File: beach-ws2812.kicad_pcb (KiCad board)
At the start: 4 copper layers, 260 x 120 mm, 183 parts, among them CON101 BARREL_JACK, P101 CONN_01X03, SW101 Pushbutton, SW102 Pushbutton, U101 STM32F103C(8-B)Tx, U102 LM1117-3.3, U103 MAX811, X101 8MHz

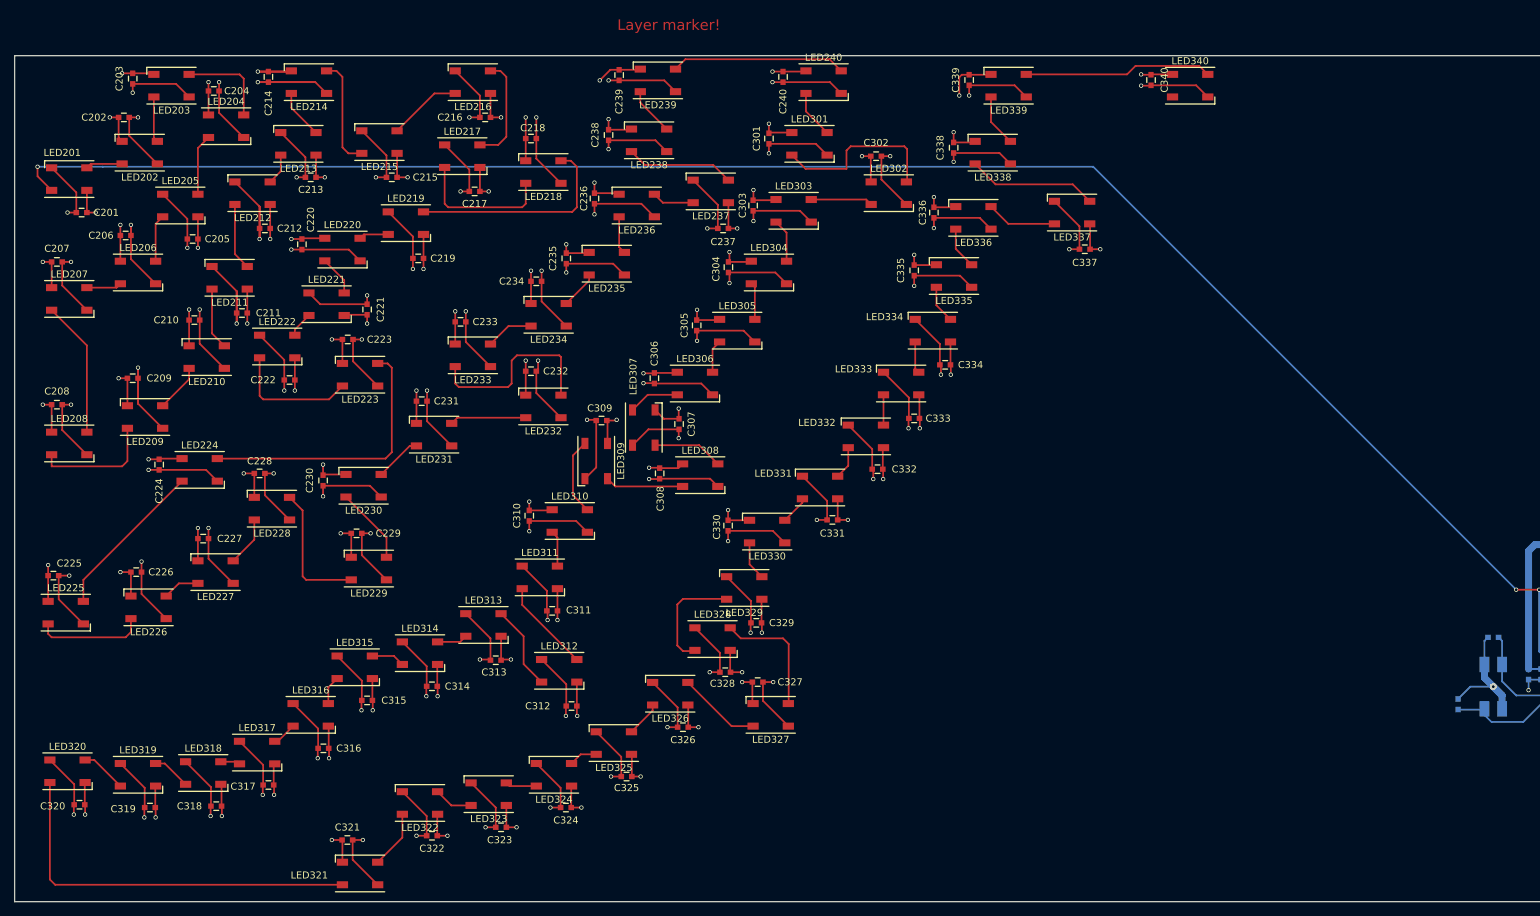
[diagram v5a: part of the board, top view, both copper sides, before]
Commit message: Now with 120 LEDs routed.
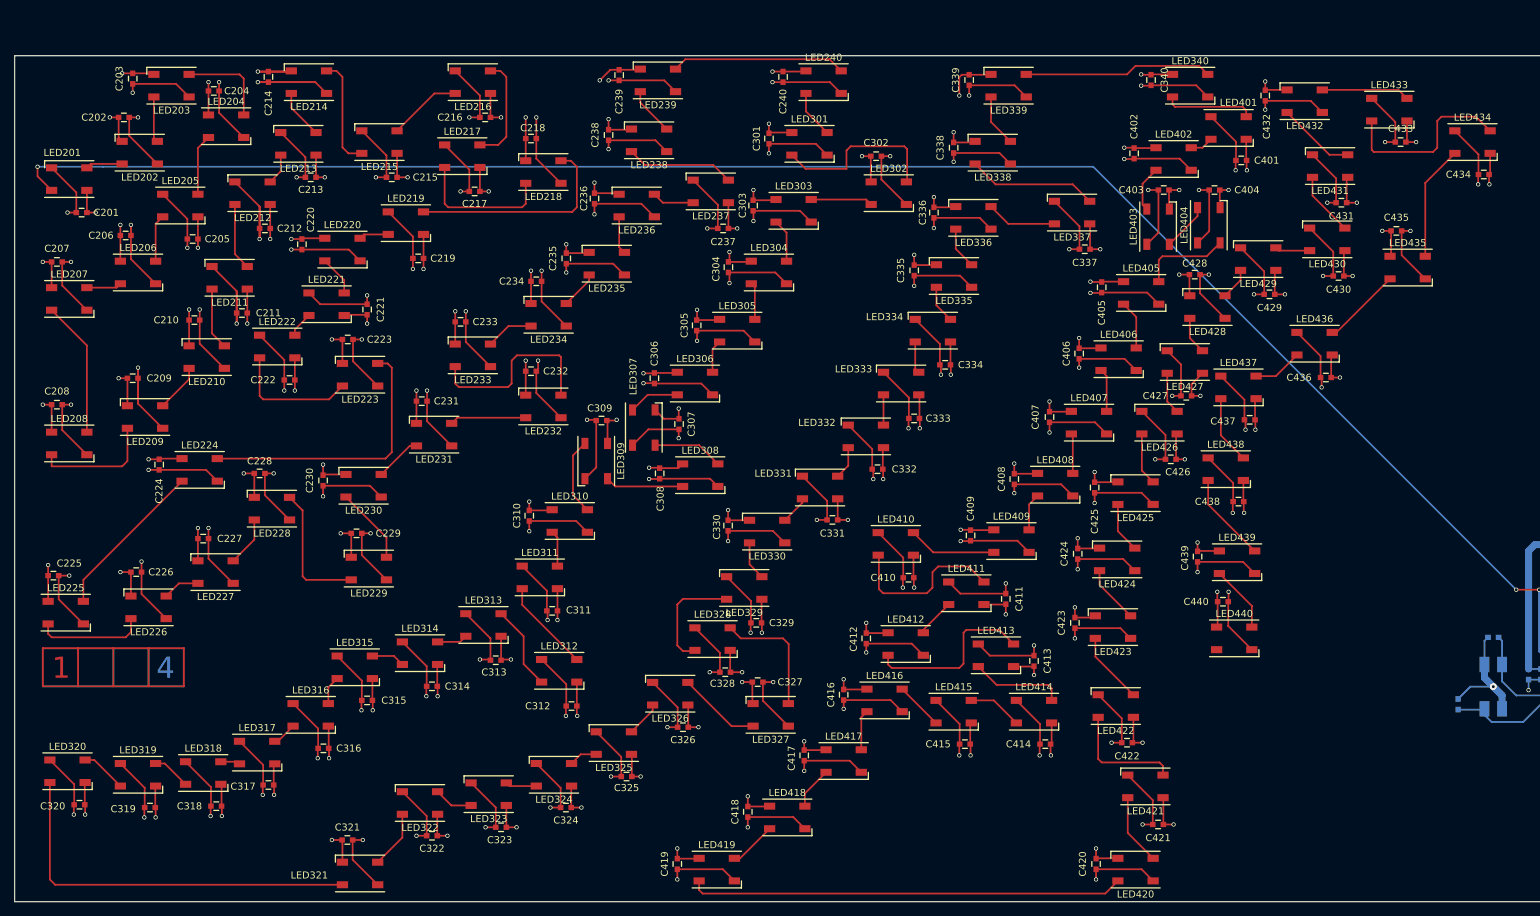
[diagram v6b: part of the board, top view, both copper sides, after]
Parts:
- added C401: 100nF, Capacitors_SMD:C_0603, F.Cu at (194.0, 33.6)
- added C402: 100nF, Capacitors_SMD:C_0603, F.Cu at (178.8, 32.6)
- added C403: 100nF, Capacitors_SMD:C_0603, F.Cu at (183.0, 37.8)
- added C404: 100nF, Capacitors_SMD:C_0603, F.Cu at (190.2, 37.8)
- added C405: 100nF, Capacitors_SMD:C_0603, F.Cu at (174.2, 51.6)
- added C406: 100nF, Capacitors_SMD:C_0603, F.Cu at (171.0, 61.0)
- added C407: 100nF, Capacitors_SMD:C_0603, F.Cu at (166.8, 70.0)
- added C408: 100nF, Capacitors_SMD:C_0603, F.Cu at (161.8, 78.8)
- added C409: 100nF, Capacitors_SMD:C_0603, F.Cu at (155.6, 86.8)
- added C410: 100nF, Capacitors_SMD:C_0603, F.Cu at (146.8, 92.8)
- added C411: 100nF, Capacitors_SMD:C_0603, F.Cu at (160.6, 95.8)
- added C412: 100nF, Capacitors_SMD:C_0603, F.Cu at (140.8, 101.4)
- added C413: 100nF, Capacitors_SMD:C_0603, F.Cu at (164.6, 104.6)
- added C414: 100nF, Capacitors_SMD:C_0603, F.Cu at (166.2, 116.4)
- added C415: 100nF, Capacitors_SMD:C_0603, F.Cu at (154.8, 116.4)
- added C416: 100nF, Capacitors_SMD:C_0603, F.Cu at (137.6, 109.4)
- added C417: 100nF, Capacitors_SMD:C_0603, F.Cu at (132.0, 118.0)
- added C418: 100nF, Capacitors_SMD:C_0603, F.Cu at (124.0, 126.0)
- added C419: 100nF, Capacitors_SMD:C_0603, F.Cu at (114.0, 133.4)
- added C420: 100nF, Capacitors_SMD:C_0603, F.Cu at (173.4, 133.4)
- added C421: 100nF, Capacitors_SMD:C_0603, F.Cu at (182.2, 127.8)
- added C422: 100nF, Capacitors_SMD:C_0603, F.Cu at (177.8, 116.2)
- added C423: 100nF, Capacitors_SMD:C_0603, F.Cu at (170.4, 99.2)
- added C424: 100nF, Capacitors_SMD:C_0603, F.Cu at (170.8, 89.4)
- added C425: 100nF, Capacitors_SMD:C_0603, F.Cu at (173.2, 80.0)
- added C426: 100nF, Capacitors_SMD:C_0603, F.Cu at (184.0, 76.0)
- added C427: 100nF, Capacitors_SMD:C_0603, F.Cu at (186.2, 67.0)
- added C428: 100nF, Capacitors_SMD:C_0603, F.Cu at (187.4, 49.8)
- added C429: 100nF, Capacitors_SMD:C_0603, F.Cu at (198.0, 52.6)
- added C430: 100nF, Capacitors_SMD:C_0603, F.Cu at (207.8, 50.0)
- added C431: 100nF, Capacitors_SMD:C_0603, F.Cu at (208.2, 39.6)
- added C432: 100nF, Capacitors_SMD:C_0603, F.Cu at (197.4, 24.4)
- added C433: 100nF, Capacitors_SMD:C_0603, F.Cu at (216.6, 31.0)
- added C434: 100nF, Capacitors_SMD:C_0603, F.Cu at (228.4, 35.6)
- added C435: 100nF, Capacitors_SMD:C_0603, F.Cu at (216.0, 43.6)
- added C436: 100nF, Capacitors_SMD:C_0603, F.Cu at (206.0, 64.4)
- added C437: 100nF, Capacitors_SMD:C_0603, F.Cu at (195.2, 70.4)
- added C438: 100nF, Capacitors_SMD:C_0603, F.Cu at (193.6, 82.0)
- added C439: 100nF, Capacitors_SMD:C_0603, F.Cu at (187.8, 89.8)
- added C440: 100nF, Capacitors_SMD:C_0603, F.Cu at (191.4, 96.2)
- added LED401: WS2812B, LEDs:LED_WS2812B-PLCC4, F.Cu at (192.2, 29.0)
- added LED402: WS2812B, LEDs:LED_WS2812B-PLCC4, F.Cu at (184.4, 33.4)
- added LED403: WS2812B, LEDs:LED_WS2812B-PLCC4, F.Cu at (182.2, 43.0)
- added LED404: WS2812B, LEDs:LED_WS2812B-PLCC4, F.Cu at (189.4, 42.8)
- added LED405: WS2812B, LEDs:LED_WS2812B-PLCC4, F.Cu at (179.8, 52.4)
- added LED406: WS2812B, LEDs:LED_WS2812B-PLCC4, F.Cu at (176.6, 61.8)
- added LED407: WS2812B, LEDs:LED_WS2812B-PLCC4, F.Cu at (172.4, 70.8)
- added LED408: WS2812B, LEDs:LED_WS2812B-PLCC4, F.Cu at (167.6, 79.6)
- added LED409: WS2812B, LEDs:LED_WS2812B-PLCC4, F.Cu at (161.4, 87.6)
- added LED410: WS2812B, LEDs:LED_WS2812B-PLCC4, F.Cu at (145.0, 88.0)
- added LED411: WS2812B, LEDs:LED_WS2812B-PLCC4, F.Cu at (155.0, 95.0)
- added LED412: WS2812B, LEDs:LED_WS2812B-PLCC4, F.Cu at (146.4, 102.2)
- added LED413: WS2812B, LEDs:LED_WS2812B-PLCC4, F.Cu at (159.2, 103.8)
- added LED414: WS2812B, LEDs:LED_WS2812B-PLCC4, F.Cu at (164.6, 111.8)
- added LED415: WS2812B, LEDs:LED_WS2812B-PLCC4, F.Cu at (153.2, 111.8)
- added LED416: WS2812B, LEDs:LED_WS2812B-PLCC4, F.Cu at (143.4, 110.2)
- added LED417: WS2812B, LEDs:LED_WS2812B-PLCC4, F.Cu at (137.6, 118.8)
- added LED418: WS2812B, LEDs:LED_WS2812B-PLCC4, F.Cu at (129.6, 126.8)
- added LED419: WS2812B, LEDs:LED_WS2812B-PLCC4, F.Cu at (119.6, 134.2)
- added LED420: WS2812B, LEDs:LED_WS2812B-PLCC4, F.Cu at (179.0, 134.2)
- added LED421: WS2812B, LEDs:LED_WS2812B-PLCC4, F.Cu at (180.4, 122.4)
- added LED422: WS2812B, LEDs:LED_WS2812B-PLCC4, F.Cu at (176.2, 111.0)
- added LED423: WS2812B, LEDs:LED_WS2812B-PLCC4, F.Cu at (175.8, 99.8)
- added LED424: WS2812B, LEDs:LED_WS2812B-PLCC4, F.Cu at (176.4, 90.2)
- added LED425: WS2812B, LEDs:LED_WS2812B-PLCC4, F.Cu at (179.0, 80.8)
- added LED426: WS2812B, LEDs:LED_WS2812B-PLCC4, F.Cu at (182.4, 70.8)
- added LED427: WS2812B, LEDs:LED_WS2812B-PLCC4, F.Cu at (186.0, 62.2)
- added LED428: WS2812B, LEDs:LED_WS2812B-PLCC4, F.Cu at (189.2, 54.4)
- added LED429: WS2812B, LEDs:LED_WS2812B-PLCC4, F.Cu at (196.4, 47.6)
- added LED430: WS2812B, LEDs:LED_WS2812B-PLCC4, F.Cu at (206.2, 44.8)
- added LED431: WS2812B, LEDs:LED_WS2812B-PLCC4, F.Cu at (206.6, 34.4)
- added LED432: WS2812B, LEDs:LED_WS2812B-PLCC4, F.Cu at (203.0, 25.2)
- added LED433: WS2812B, LEDs:LED_WS2812B-PLCC4, F.Cu at (215.0, 26.4)
- added LED434: WS2812B, LEDs:LED_WS2812B-PLCC4, F.Cu at (226.8, 31.0)
- added LED435: WS2812B, LEDs:LED_WS2812B-PLCC4, F.Cu at (217.6, 48.8)
- added LED436: WS2812B, LEDs:LED_WS2812B-PLCC4, F.Cu at (204.4, 59.6)
- added LED437: WS2812B, LEDs:LED_WS2812B-PLCC4, F.Cu at (193.6, 65.8)
- added LED438: WS2812B, LEDs:LED_WS2812B-PLCC4, F.Cu at (191.8, 77.4)
- added LED439: WS2812B, LEDs:LED_WS2812B-PLCC4, F.Cu at (193.4, 90.6)
- added LED440: WS2812B, LEDs:LED_WS2812B-PLCC4, F.Cu at (193.0, 101.4)
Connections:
- LED340 pad 2: Net-(LED340-Pad2) -> LEDDATA3
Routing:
- net GND: track 731.1 -> 1032.6 mm, vias 91 -> 131
- net +5V: track 671.5 -> 962.5 mm, vias 81 -> 121
- net (no net): track 0.50 -> 268.0 mm
- net Net-(LED419-Pad2): track 0.00 -> 61.7 mm
- net Net-(LED433-Pad2): track 0.00 -> 26.1 mm
- net Net-(LED412-Pad2): track 0.00 -> 24.9 mm
- net Net-(LED410-Pad2): track 0.00 -> 23.8 mm
- net Net-(LED421-Pad2): track 0.00 -> 16.8 mm
- net Net-(LED434-Pad2): track 0.00 -> 16.3 mm
- net Net-(LED413-Pad2): track 0.00 -> 13.4 mm
- net Net-(LED404-Pad2): track 0.00 -> 12.8 mm
- net LEDDATA3: track 0.00 -> 12.8 mm
- net Net-(LED438-Pad2): track 0.00 -> 12.7 mm
- net Net-(LED409-Pad2): track 0.00 -> 12.6 mm
- net Net-(LED432-Pad2): track 0.00 -> 12.5 mm
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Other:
- board text added: "1"
- board text added: "2"
- board text added: "3"
- board text added: "4"
- board text removed: "Layer marker!"

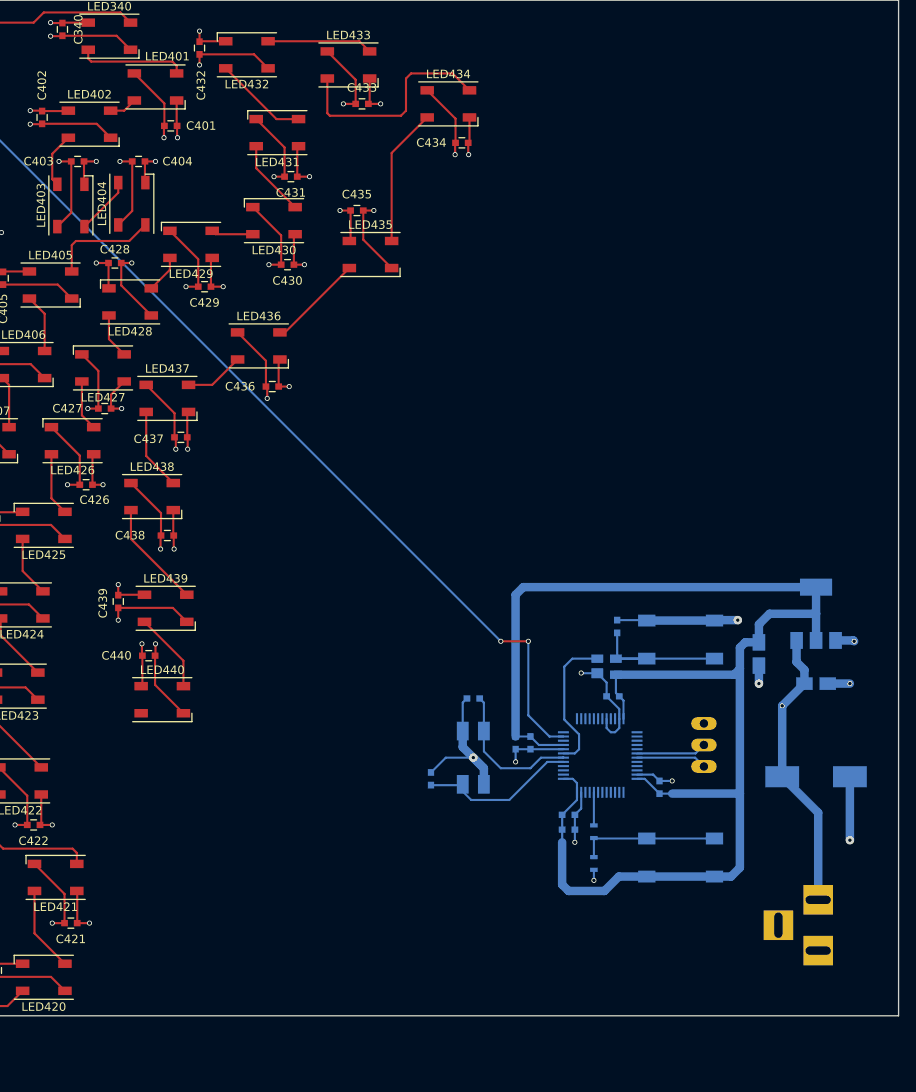
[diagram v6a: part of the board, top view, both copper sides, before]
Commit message: Placed 160 LEDs (caps missing for the last 40).
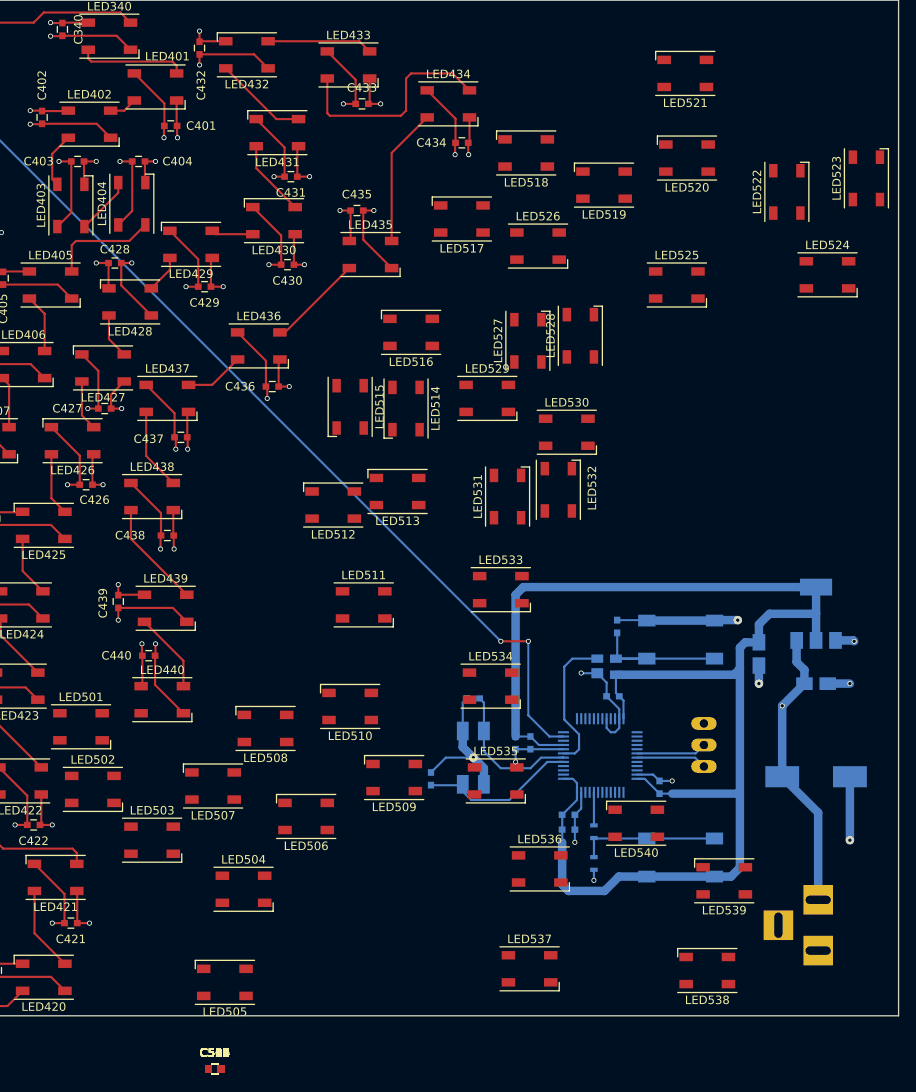
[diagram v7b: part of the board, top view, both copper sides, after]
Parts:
- added C501, C502, C503, C504, C505, C506, C507, C508, C509, C510, C511, C512, C513, C514, C515, C516, C517, C518, C519, C520, C521, C522, C523, C524, C525, C526, C527, C528, C529, C530, C531, C532, C533, C534, C535, C536, C537, C538, C539, C540: 100nF, Capacitors_SMD:C_0603, F.Cu at (199.2, 145.0)
- added LED501: WS2812B, LEDs:LED_WS2812B-PLCC4, F.Cu at (183.4, 104.6)
- added LED502: WS2812B, LEDs:LED_WS2812B-PLCC4, F.Cu at (184.8, 112.0)
- added LED503: WS2812B, LEDs:LED_WS2812B-PLCC4, F.Cu at (191.8, 118.0)
- added LED504: WS2812B, LEDs:LED_WS2812B-PLCC4, F.Cu at (202.6, 123.8)
- added LED505: WS2812B, LEDs:LED_WS2812B-PLCC4, F.Cu at (200.4, 134.8)
- added LED506: WS2812B, LEDs:LED_WS2812B-PLCC4, F.Cu at (210.0, 115.2)
- added LED507: WS2812B, LEDs:LED_WS2812B-PLCC4, F.Cu at (199.0, 111.6)
- added LED508: WS2812B, LEDs:LED_WS2812B-PLCC4, F.Cu at (205.2, 104.8)
- added LED509: WS2812B, LEDs:LED_WS2812B-PLCC4, F.Cu at (220.4, 110.6)
- added LED510: WS2812B, LEDs:LED_WS2812B-PLCC4, F.Cu at (215.2, 102.2)
- added LED511: WS2812B, LEDs:LED_WS2812B-PLCC4, F.Cu at (216.8, 90.2)
- added LED512: WS2812B, LEDs:LED_WS2812B-PLCC4, F.Cu at (213.2, 78.4)
- added LED513: WS2812B, LEDs:LED_WS2812B-PLCC4, F.Cu at (220.8, 76.8)
- added LED514: WS2812B, LEDs:LED_WS2812B-PLCC4, F.Cu at (221.8, 67.0)
- added LED515: WS2812B, LEDs:LED_WS2812B-PLCC4, F.Cu at (215.2, 66.8)
- added LED516: WS2812B, LEDs:LED_WS2812B-PLCC4, F.Cu at (222.4, 58.0)
- added LED517: WS2812B, LEDs:LED_WS2812B-PLCC4, F.Cu at (228.4, 44.6)
- added LED518: WS2812B, LEDs:LED_WS2812B-PLCC4, F.Cu at (236.0, 36.8)
- added LED519: WS2812B, LEDs:LED_WS2812B-PLCC4, F.Cu at (245.2, 40.6)
- added LED520: WS2812B, LEDs:LED_WS2812B-PLCC4, F.Cu at (255.0, 37.4)
- added LED521: WS2812B, LEDs:LED_WS2812B-PLCC4, F.Cu at (254.8, 27.4)
- added LED522: WS2812B, LEDs:LED_WS2812B-PLCC4, F.Cu at (266.8, 41.4)
- added LED523: WS2812B, LEDs:LED_WS2812B-PLCC4, F.Cu at (276.2, 39.8)
- added LED524: WS2812B, LEDs:LED_WS2812B-PLCC4, F.Cu at (271.6, 51.2)
- added LED525: WS2812B, LEDs:LED_WS2812B-PLCC4, F.Cu at (253.8, 52.4)
- added LED526: WS2812B, LEDs:LED_WS2812B-PLCC4, F.Cu at (237.4, 47.8)
- added LED527: WS2812B, LEDs:LED_WS2812B-PLCC4, F.Cu at (236.2, 59.0)
- added LED528: WS2812B, LEDs:LED_WS2812B-PLCC4, F.Cu at (242.4, 58.4)
- added LED529: WS2812B, LEDs:LED_WS2812B-PLCC4, F.Cu at (231.4, 65.8)
- added LED530: WS2812B, LEDs:LED_WS2812B-PLCC4, F.Cu at (240.8, 69.8)
- added LED531: WS2812B, LEDs:LED_WS2812B-PLCC4, F.Cu at (233.8, 77.4)
- added LED532: WS2812B, LEDs:LED_WS2812B-PLCC4, F.Cu at (239.8, 76.6)
- added LED533: WS2812B, LEDs:LED_WS2812B-PLCC4, F.Cu at (233.0, 88.4)
- added LED534: WS2812B, LEDs:LED_WS2812B-PLCC4, F.Cu at (231.8, 99.8)
- added LED535: WS2812B, LEDs:LED_WS2812B-PLCC4, F.Cu at (232.4, 111.0)
- added LED536: WS2812B, LEDs:LED_WS2812B-PLCC4, F.Cu at (237.6, 121.4)
- added LED537: WS2812B, LEDs:LED_WS2812B-PLCC4, F.Cu at (236.4, 133.2)
- added LED538: WS2812B, LEDs:LED_WS2812B-PLCC4, F.Cu at (257.4, 133.4)
- added LED539: WS2812B, LEDs:LED_WS2812B-PLCC4, F.Cu at (259.4, 122.8)
- added LED540: WS2812B, LEDs:LED_WS2812B-PLCC4, F.Cu at (249.0, 116.0)
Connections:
- LED440 pad 2: Net-(LED440-Pad2) -> LEDDATA4
